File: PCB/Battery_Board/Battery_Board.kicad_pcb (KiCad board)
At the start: 2 copper layers, 90 x 83.5 mm, 4 parts, among them J1 SE2-30

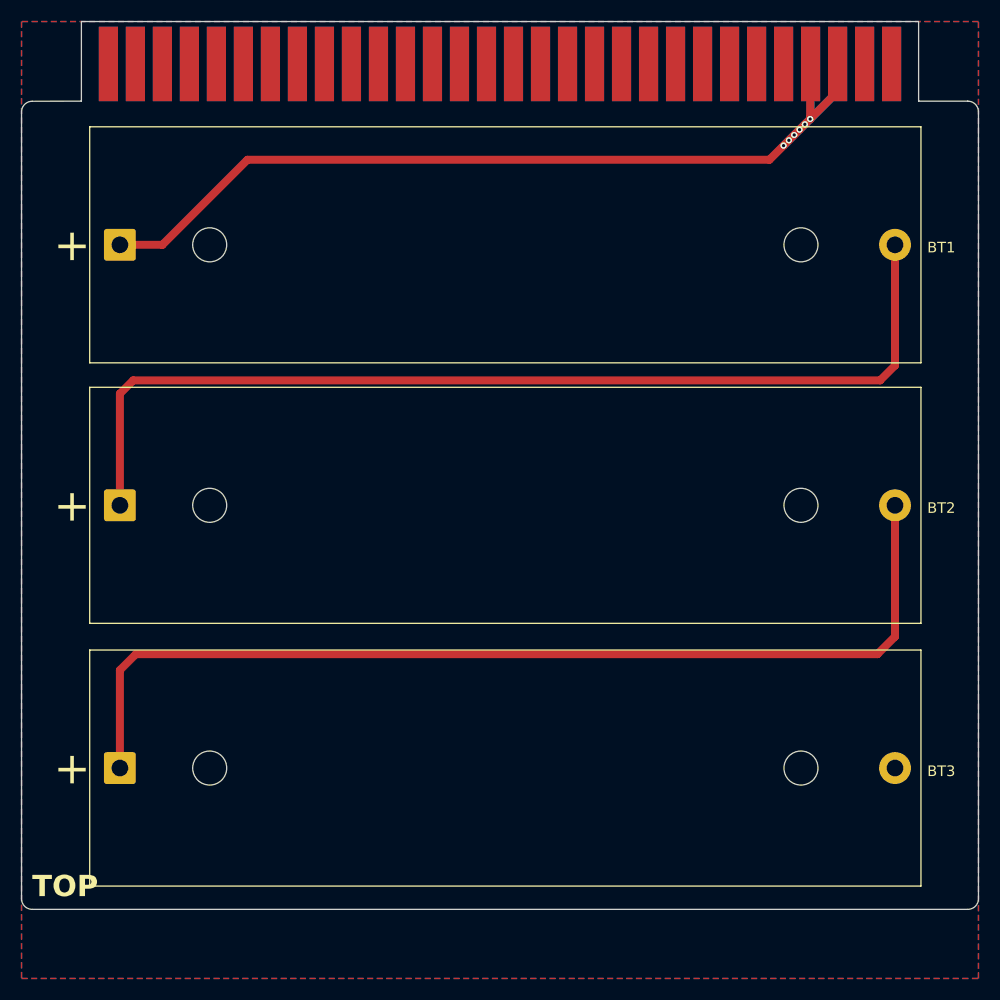
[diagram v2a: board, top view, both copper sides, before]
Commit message: Added ideal diode to battery board, cleaned up battery board layout
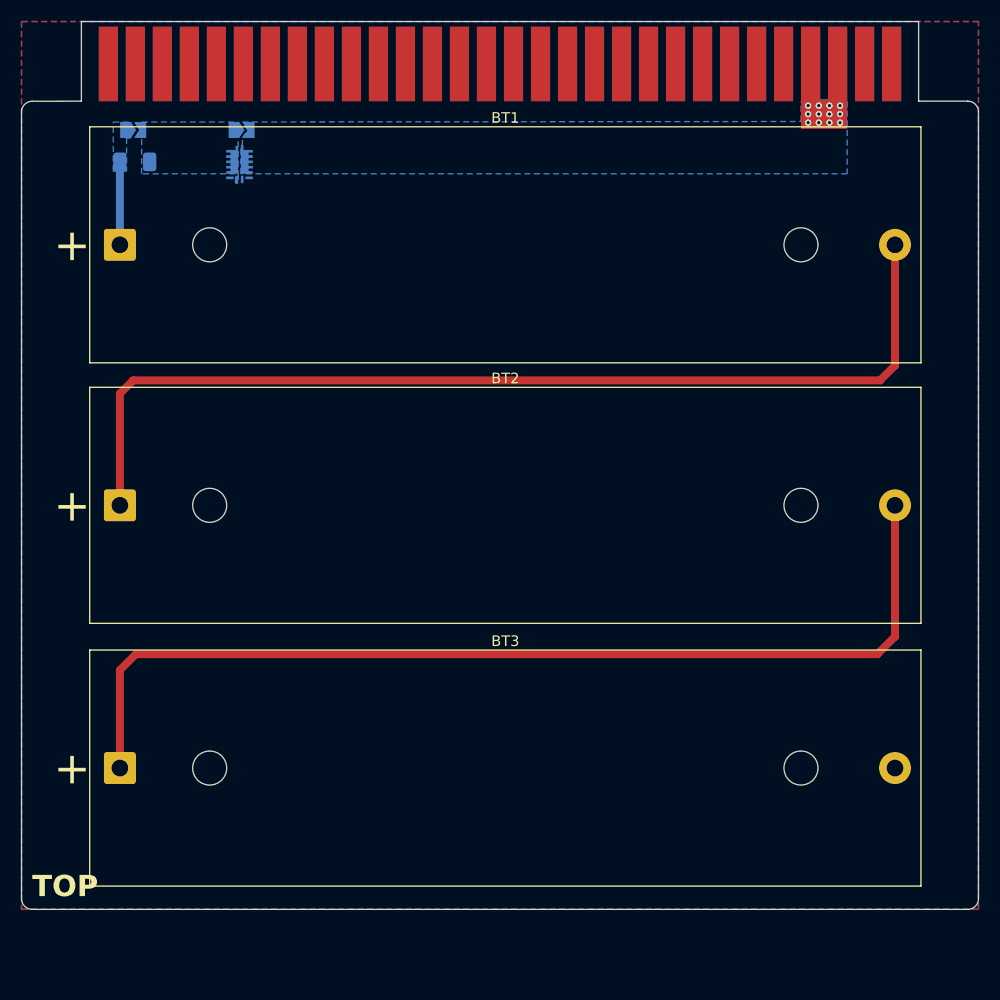
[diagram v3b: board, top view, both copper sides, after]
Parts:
- added Diode BP: SolderJumper_2_Open, Jumper:SolderJumper-2_P1.3mm_Open_TrianglePad1.0x1.5mm, B.Cu at (193.2, 52.2)
- added F1: Fuse_Small, Fuse:Fuse_1206_3216Metric, B.Cu at (183.2, 55.2)
- added Fuse BP: SolderJumper_2_Open, Jumper:SolderJumper-2_P1.3mm_Open_TrianglePad1.0x1.5mm, B.Cu at (183.0, 52.2)
- added U1: LTC4451AV-TRPBF, SE2-30:05-08-1683_ADI, B.Cu at (193.0, 55.5)
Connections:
- BT1 pad 1: VBUS -> +BATT
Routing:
- net VBUS: track 96.2 -> 5.26 mm, vias 6 -> 12
- net +BATT: track 0.00 -> 7.80 mm
- added copper zone on B.Cu, net +BATT
- added copper zone on B.Cu, net Net-(JP1-B)
- added copper zone on B.Cu, net VBUS
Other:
- board text removed: "Designed by: Yen Do Manas Moondra Grant Gardner"
